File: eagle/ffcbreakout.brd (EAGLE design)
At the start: 15.2 x 30.5 mm, 18 parts

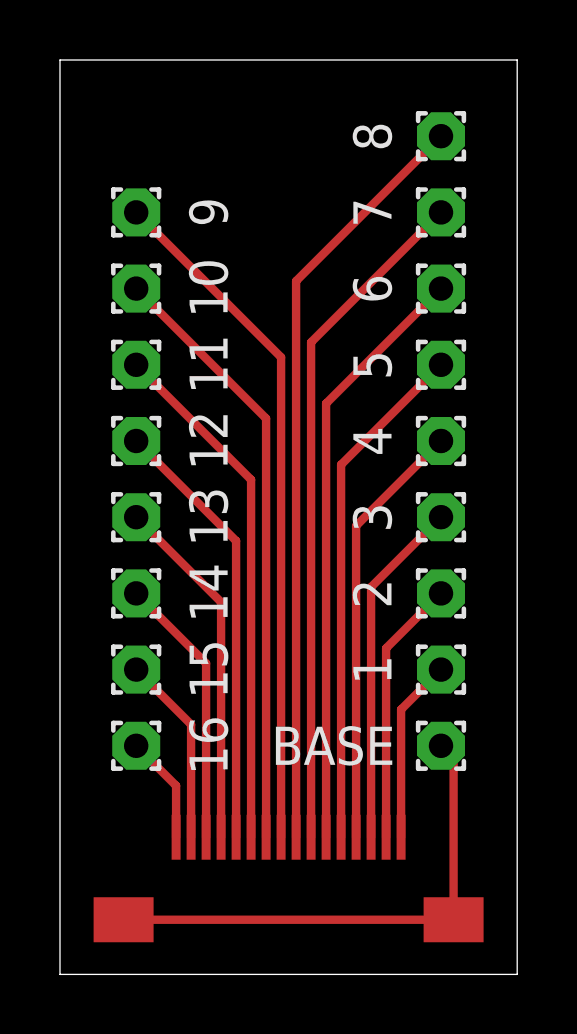
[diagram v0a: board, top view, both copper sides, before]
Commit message: First order of probe, probebase and FFC breakout PCBs for 22mm enclosure
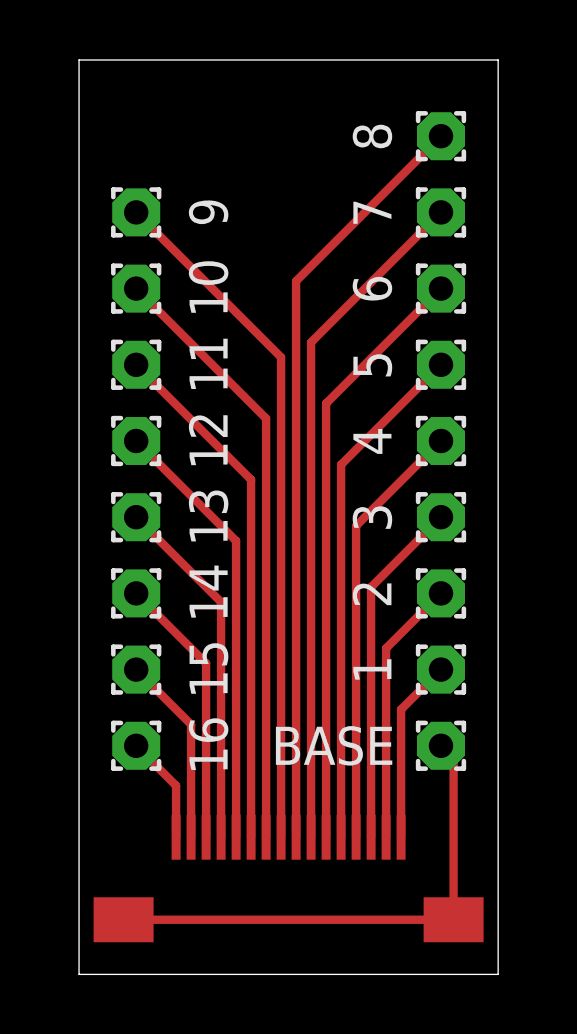
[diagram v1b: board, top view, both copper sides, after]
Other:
- board size 15.2 x 30.5 mm -> 14 x 30.5 mm
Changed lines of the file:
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@@
 <board>
 <plain>
-<wire x1="0" y1="0" x2="15.24" y2="0" width="0" layer="20"/>
-<wire x1="15.24" y1="0" x2="15.24" y2="30.48" width="0" layer="20"/>
-<wire x1="15.24" y1="30.48" x2="0" y2="30.48" width="0" layer="20"/>
-<wire x1="0" y1="30.48" x2="0" y2="0" width="0" layer="20"/>
+<wire x1="0.635" y1="0" x2="14.605" y2="0" width="0" layer="20"/>
+<wire x1="14.605" y1="0" x2="14.605" y2="30.48" width="0" layer="20"/>
+<wire x1="14.605" y1="30.48" x2="0.635" y2="30.48" width="0" layer="20"/>
+<wire x1="0.635" y1="30.48" x2="0.635" y2="0" width="0" layer="20"/>
 </plain>
 <attributes>
@@
 </class>
 </classes>
-<designrules name="default">
+<designrules name="default *">
 <description language="de">&lt;b&gt;EAGLE Design Rules&lt;/b&gt;
 &lt;p&gt;
@@
 <param name="mdViaViaSameLayer" value="6mil"/>
 <param name="mnLayersViaInSmd" value="2"/>
-<param name="mdCopperDimension" value="40mil"/>
+<param name="mdCopperDimension" value="10mil"/>
 <param name="mdDrill" value="6mil"/>
 <param name="mdSmdStop" value="0mil"/>
